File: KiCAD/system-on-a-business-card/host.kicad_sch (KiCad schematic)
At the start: 23 parts, among them SW2 SW_Push, U2 ESP32-C3, U3 ZD25WQ32C, Y1 40MHz

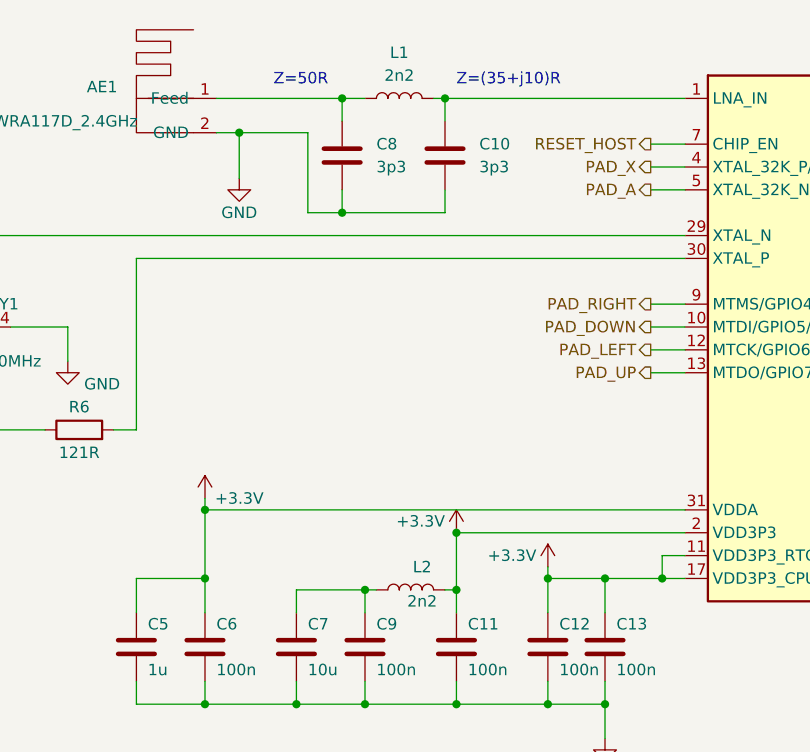
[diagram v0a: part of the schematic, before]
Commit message: fixed #12 connected OLED VDD pins to 3.3V power line
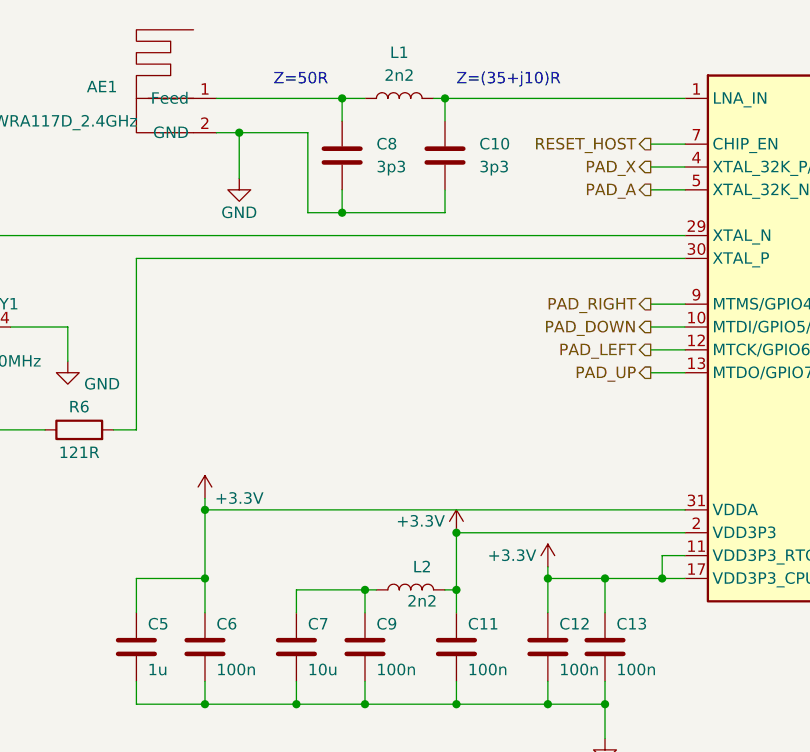
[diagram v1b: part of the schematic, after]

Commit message: fixes #11: Footprint of Flash IC corrected
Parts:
- U3: footprint Package_SO:SOP-8_3.9x4.9mm_P1.27mm -> Package_SO:SOP-8_5.28x5.23mm_P1.27mm
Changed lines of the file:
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@@
       (effects (font (size 1.27 1.27)))
     )
-    (property "Footprint" "Package_SO:SOP-8_3.9x4.9mm_P1.27mm" (at 236.22 39.37 0)
+    (property "Footprint" "Package_SO:SOP-8_5.28x5.23mm_P1.27mm" (at 236.22 39.37 0)
       (effects (font (size 1.27 1.27)) hide)
     )

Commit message: #10: added buzzer, io-expander, removed transistors from resistive pad cirucit
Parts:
- added BZ1: Buzzer, symbol Device:Buzzer
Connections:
- net GND: now also BZ1.2 (+)
- net PAD_A: no longer names the net of U2.5 (XTAL_32K_N/ADC1_CH1)
- net PAD_B: no longer names the net of U2.6 (GPIO2/ADC1_CH2)
- net PAD_DOWN: no longer names the net of U2.10 (MTDI/GPIO5/ADC2_CH0)
- net PAD_LEFT renamed DISPLAY_RESET
- net PAD_RIGHT: no longer names the net of U2.9 (MTMS/GPIO4/ADC1_CH4)
- net PAD_UP: no longer names the net of U2.13 (MTDO/GPIO7)
- net PAD_UP: now also BZ1.1 (-)
- net PAD_X renamed IO_EXP_INT
- net PAD_Y: no longer names the net of U2.28 (U0TXD/GPIO21)
- net SELECT: no longer names the net of U2.8 (GPIO3/ADC1_CH3)
- net START: no longer names the net of U2.27 (U0RXD/GPIO20)
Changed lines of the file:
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@@
-    (stroke (width 0) (type default))
-  )
-  (wire (pts (xy 123.19 62.23) (xy 127 62.23))
     (stroke (width 0) (type default))
   )
@@
     (stroke (width 0) (type default))
   )
+  (wire (pts (xy 121.92 68.58) (xy 121.92 67.31))
+    (stroke (width 0) (type default))
+  )
   (wire (pts (xy 73.66 96.52) (xy 73.66 99.06))
     (stroke (width 0) (type default))
@@
     (stroke (width 0) (type default))
   )
-  (wire (pts (xy 123.19 54.61) (xy 127 54.61))
-    (stroke (width 0) (type default))
-  )
   (wire (pts (xy 74.93 35.56) (xy 77.47 35.56))
     (stroke (width 0) (type default))
@@
     (stroke (width 0) (type default))
   )
-  (wire (pts (xy 182.88 34.29) (xy 186.69 34.29))
-    (stroke (width 0) (type default))
-  )
   (wire (pts (xy 257.81 43.18) (xy 257.81 39.37))
     (stroke (width 0) (type default))
@@
     (stroke (width 0) (type default))
   )
-  (wire (pts (xy 186.69 77.47) (xy 182.88 77.47))
-    (stroke (width 0) (type default))
-  )
   (wire (pts (xy 100.33 44.45) (xy 88.9 44.45))
     (stroke (width 0) (type default))
   )
-  (wire (pts (xy 182.88 31.75) (xy 186.69 31.75))
-    (stroke (width 0) (type default))
-  )
   (wire (pts (xy 66.04 99.06) (xy 73.66 99.06))
     (stroke (width 0) (type default))
@@
     (stroke (width 0) (type default))
   )
+  (wire (pts (xy 123.19 39.37) (xy 127 39.37))
+    (stroke (width 0) (type default))
+  )
   (wire (pts (xy 182.88 85.09) (xy 186.69 85.09))
     (stroke (width 0) (type default))
@@
     (stroke (width 0) (type default))
   )
-  (wire (pts (xy 186.69 74.93) (xy 182.88 74.93))
-    (stroke (width 0) (type default))
-  )
   (wire (pts (xy 83.82 96.52) (xy 83.82 99.06))
     (stroke (width 0) (type default))
@@
     (stroke (width 0) (type default))
   )
-  (wire (pts (xy 123.19 39.37) (xy 127 39.37))
-    (stroke (width 0) (type default))
-  )
   (wire (pts (xy 118.11 85.09) (xy 124.46 85.09))
     (stroke (width 0) (type default))
@@
     (stroke (width 0) (type default))
   )
-  (wire (pts (xy 123.19 41.91) (xy 127 41.91))
-    (stroke (width 0) (type default))
-  )
   (wire (pts (xy 46.99 46.99) (xy 46.99 53.34))
     (stroke (width 0) (type default))
@@
     (stroke (width 0) (type default))
   )
-  (wire (pts (xy 123.19 59.69) (xy 127 59.69))
-    (stroke (width 0) (type default))
-  )
   (wire (pts (xy 88.9 31.75) (xy 91.44 31.75))
     (stroke (width 0) (type default))
   )
-  (wire (pts (xy 123.19 57.15) (xy 127 57.15))
-    (stroke (width 0) (type default))
-  )
   (wire (pts (xy 182.88 62.23) (xy 220.98 62.23))
     (stroke (width 0) (type default))
@@
     (stroke (width 0) (type default))
   )
+  (wire (pts (xy 120.65 59.69) (xy 127 59.69))
+    (stroke (width 0) (type default))
+  )
   (wire (pts (xy 85.09 35.56) (xy 85.09 44.45))
     (stroke (width 0) (type default))
@@
   )
   (wire (pts (xy 220.98 132.08) (xy 220.98 134.62))
+    (stroke (width 0) (type default))
+  )
+  (wire (pts (xy 121.92 62.23) (xy 127 62.23))
     (stroke (width 0) (type default))
   )
@@
     )
   )
-  (hierarchical_label "SELECT" (shape output) (at 186.69 74.93 0) (fields_autoplaced)
-    (effects (font (size 1.27 1.27)) (justify left))
-  )
   (hierarchical_label "RESET_HOST" (shape output) (at 123.19 36.83 180) (fields_autoplaced)
     (effects (font (size 1.27 1.27)) (justify right))
@@
     (effects (font (size 1.27 1.27)) (justify left))
   )
-  (hierarchical_label "PAD_LEFT" (shape output) (at 123.19 59.69 180) (fields_autoplaced)
-    (effects (font (size 1.27 1.27)) (justify right))
-  )
-  (hierarchical_label "PAD_B" (shape output) (at 186.69 77.47 0) (fields_autoplaced)
-    (effects (font (size 1.27 1.27)) (justify left))
-  )
-  (hierarchical_label "PAD_RIGHT" (shape output) (at 123.19 54.61 180) (fields_autoplaced)
-    (effects (font (size 1.27 1.27)) (justify right))
-  )
-  (hierarchical_label "PAD_A" (shape output) (at 123.19 41.91 180) (fields_autoplaced)
-    (effects (font (size 1.27 1.27)) (justify right))
-  )
-  (hierarchical_label "PAD_X" (shape output) (at 123.19 39.37 180) (fields_autoplaced)
-    (effects (font (size 1.27 1.27)) (justify right))
-  )
   (hierarchical_label "I2C_SDA" (shape bidirectional) (at 186.69 72.39 0) (fields_autoplaced)
     (effects (font (size 1.27 1.27)) (justify left))
   )
-  (hierarchical_label "PAD_UP" (shape output) (at 123.19 62.23 180) (fields_autoplaced)
-    (effects (font (size 1.27 1.27)) (justify right))
-  )
   (hierarchical_label "USB_D-" (shape bidirectional) (at 186.69 41.91 0) (fields_autoplaced)
     (effects (font (size 1.27 1.27)) (justify left))
   )
-  (hierarchical_label "PAD_Y" (shape output) (at 186.69 31.75 0) (fields_autoplaced)
-    (effects (font (size 1.27 1.27)) (justify left))
-  )
-  (hierarchical_label "PAD_DOWN" (shape output) (at 123.19 57.15 180) (fields_autoplaced)
-    (effects (font (size 1.27 1.27)) (justify right))
-  )
   (hierarchical_label "I2C_SCL" (shape output) (at 186.69 67.31 0) (fields_autoplaced)
     (effects (font (size 1.27 1.27)) (justify left))
   )
-  (hierarchical_label "START" (shape output) (at 186.69 34.29 0) (fields_autoplaced)
-    (effects (font (size 1.27 1.27)) (justify left))
+  (hierarchical_label "IO_EXP_INT" (shape input) (at 123.19 39.37 180) (fields_autoplaced)
+    (effects (font (size 1.27 1.27)) (justify right))
+  )
+  (hierarchical_label "DISPLAY_RESET" (shape input) (at 120.65 59.69 180) (fields_autoplaced)
+    (effects (font (size 1.27 1.27)) (justify right))
   )
   (symbol (lib_id "power:+3.3V") (at 101.6 80.01 0) (unit 1)
@@
     )
   )
+  (symbol (lib_id "power:GND") (at 121.92 68.58 0) (unit 1)
+    (in_bom yes) (on_board yes) (dnp no) (fields_autoplaced)
+    (property "Reference" "#PWR050" (at 121.92 74.93 0)
+      (effects (font (size 1.27 1.27)) hide)
+    )
+    (property "Value" "GND" (at 121.92 73.66 0)
+      (effects (font (size 1.27 1.27)))
+    )
+    (property "Footprint" "" (at 121.92 68.58 0)
+      (effects (font (size 1.27 1.27)) hide)
+    )
+    (property "Datasheet" "" (at 121.92 68.58 0)
+      (effects (font (size 1.27 1.27)) hide)
+    )
+    (pin "1")
+    (instances
+      (project "system-on-a-business-card"
+        (path "/49855302-2ecc-4f42-8bbd-b9c2e284f529/d51daf21-f243-4884-8481-74d26cfa222b"
+          (reference "#PWR050") (unit 1)
+        )
+      )
+    )
+  )
   (symbol (lib_id "power:GND") (at 36.83 60.96 0) (unit 1)
     (in_bom yes) (on_board yes) (dnp no)
@@
         )
       )
+    )
+  )
+  (symbol (lib_id "Device:Buzzer") (at 119.38 64.77 0) (mirror y) (unit 1)
+    (in_bom yes) (on_board yes) (dnp no)
+    (property "Reference" "BZ1" (at 115.57 63.5 0)
+      (effects (font (size 1.27 1.27)) (justify left))
+    )
+    (property "Value" "Buzzer" (at 115.57 66.04 0)
+      (effects (font (size 1.27 1.27)) (justify left))
+    )
+    (property "Footprint" "" (at 120.015 62.23 90)
+      (effects (font (size 1.27 1.27)) hide)
+    )
+    (property "Datasheet" "~" (at 120.015 62.23 90)
+      (effects (font (size 1.27 1.27)) hide)
+    )
+    (pin "1")
+    (pin "2")
+    (instances
+      (project "system-on-a-business-card"
+        (path "/49855302-2ecc-4f42-8bbd-b9c2e284f529/d51daf21-f243-4884-8481-74d26cfa222b"
+          (reference "BZ1") (unit 1)
+        )
+      )

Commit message: #10: removed on/off switch again, started working on layout
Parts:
- BZ1: footprint (none) -> Buzzer_Beeper:Buzzer_Mallory_AST1109MLTRQ
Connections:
- net IO_EXP_INT: now also U2.10 (MTDI/GPIO5/ADC2_CH0); no longer U2.4 (XTAL_32K_P/ADC1_CH0)
- net UART_RXD: now reaches U2.27 (U0RXD/GPIO20)
- net UART_TXD: now reaches U2.28 (U0TXD/GPIO21)
- no-connect marks 0 -> 5
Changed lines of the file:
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@@
   (junction (at 91.44 99.06) (diameter 0) (color 0 0 0 0)
   )
+  (no_connect (at 182.88 77.47))
+  (no_connect (at 127 39.37))
+  (no_connect (at 127 54.61))
+  (no_connect (at 182.88 74.93))
+  (no_connect (at 127 41.91))
   (wire (pts (xy 73.66 77.47) (xy 73.66 85.09))
     (stroke (width 0) (type default))
@@
     (stroke (width 0) (type default))
   )
+  (wire (pts (xy 186.69 31.75) (xy 182.88 31.75))
+    (stroke (width 0) (type default))
+  )
   (wire (pts (xy 74.93 35.56) (xy 77.47 35.56))
     (stroke (width 0) (type default))
@@
     (stroke (width 0) (type default))
   )
-  (wire (pts (xy 123.19 39.37) (xy 127 39.37))
+  (wire (pts (xy 120.65 57.15) (xy 127 57.15))
     (stroke (width 0) (type default))
   )
@@
   )
   (wire (pts (xy 111.76 83.82) (xy 111.76 85.09))
+    (stroke (width 0) (type default))
+  )
+  (wire (pts (xy 186.69 34.29) (xy 182.88 34.29))
     (stroke (width 0) (type default))
   )
@@
     (effects (font (size 1.27 1.27)) (justify left))
   )
+  (hierarchical_label "UART_RXD" (shape output) (at 186.69 34.29 0) (fields_autoplaced)
+    (effects (font (size 1.27 1.27)) (justify left))
+  )
   (hierarchical_label "I2C_SCL" (shape output) (at 186.69 67.31 0) (fields_autoplaced)
     (effects (font (size 1.27 1.27)) (justify left))
   )
-  (hierarchical_label "IO_EXP_INT" (shape input) (at 123.19 39.37 180) (fields_autoplaced)
+  (hierarchical_label "UART_TXD" (shape input) (at 186.69 31.75 0) (fields_autoplaced)
+    (effects (font (size 1.27 1.27)) (justify left))
+  )
+  (hierarchical_label "IO_EXP_INT" (shape input) (at 120.65 57.15 180) (fields_autoplaced)
     (effects (font (size 1.27 1.27)) (justify right))
   )
@@
       (effects (font (size 1.27 1.27)) (justify left))
     )
-    (property "Footprint" "" (at 120.015 62.23 90)
-      (effects (font (size 1.27 1.27)) hide)
-    )
+    (property "Footprint" "Buzzer_Beeper:Buzzer_Mallory_AST1109MLTRQ" (at 120.015 62.23 90)
+      (effects (font (size 1.27 1.27)) hide)
+    )
